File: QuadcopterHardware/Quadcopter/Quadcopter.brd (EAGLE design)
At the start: 47 x 28 mm, 47 parts, among them J2 FTDI_DEVICERA_SMT, M1 WIRELESS-NRF24L01, U1 ATMEGA328P_TQFP, U3 GY-521MPU6050

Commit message: getting there
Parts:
- removed J2: FTDI_DEVICERA_SMT, quad:FTDI_DEVICE_RA_SMT
- added J1: FTDI_DEVICE, quad:FTDI_DEVICE_SIDE
- moved C14 7.04 mm to (7.06, 30.6)
- moved R6 3.88 mm to (8.28, 15.5), turned to 90 degrees
- moved C9 3.01 mm to (6.21, 23.2)
- moved C6 2.19 mm to (6.25, 13.5), turned to 270 degrees
- moved S1 0.57 mm to (3.96, 6.59)
- moved U3 0.26 mm to (23.3, 16.0)
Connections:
- net 3V3: now also J1.P$4; no longer J2.4
- net DTR: now also J1.P$1; no longer J2.1
- net GND: now also J1.P$5, J1.P$6; no longer J2.5, J2.6
- net UART_RX: now also J1.P$3; no longer J2.3
- net UART_TX: now also J1.P$2; no longer J2.2
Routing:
- net RST: track 9.72 -> 36.7 mm, vias 0 -> 2
- net VBATT: track 73.2 -> 47.4 mm
- net ACC_INT: track 0.00 -> 21.7 mm
- net UART_RX: track 0.00 -> 18.4 mm, vias 0 -> 2
- net 3V3: track 77.6 -> 95.3 mm
- net UART_TX: track 0.00 -> 16.6 mm, vias 0 -> 2
- net DTR: track 11.6 -> 3.00 mm, vias 1 -> 0
- net SCL: track 0.00 -> 8.02 mm
- net SDA: track 0.00 -> 6.52 mm
- net GND: track 46.9 -> 44.3 mm

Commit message: draft 1 done, needs checking
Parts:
- removed LED2, LED3: RED, led:CHIP-LED0603
- removed R1, R3: 150, rcl:R0603
- moved LED1 58.8 mm to (27.1, 22.3)
- moved R4 56.8 mm to (32.2, 22.3)
- moved C14 7.42 mm to (6.21, 23.2), flipped to the bottom
- moved C6 3.21 mm to (8.98, 11.9)
- moved R6 2.90 mm to (6.12, 13.6)
- moved R8 1.56 mm to (35.8, 23.2)
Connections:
- removed net LED2: LED2.A, U1.25
- removed net LED3: LED3.A, U1.26
- removed net N$2: LED2.C, R3.1
- removed net N$3: LED3.C, R4.1
- removed net N$5: LED1.C, R1.1
- new net LEDRESISTOR: LED1.C, R4.1
- net GND: no longer R1.2, R3.2
- net LED1: now also U1.26; no longer U1.24
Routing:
- net 3V3: track 95.3 -> 112.7 mm, vias 2 -> 3
- net UART_TX: track 16.6 -> 25.7 mm
- net RST: track 36.7 -> 45.3 mm
- net UART_RX: track 18.4 -> 26.7 mm
- net GND: track 44.3 -> 48.5 mm
- net LEDRESISTOR: track 0.00 -> 3.52 mm
- net DTR: track 3.00 -> 5.03 mm
- net N$5: track 1.70 -> 0.00 mm
- net N$2: track 1.58 -> 0.00 mm
- net VDIV: track 7.76 -> 9.30 mm
- net ACC_INT: track 21.7 -> 20.2 mm
- net N$3: track 1.49 -> 0.00 mm
- net LED1: track 0.00 -> 1.37 mm

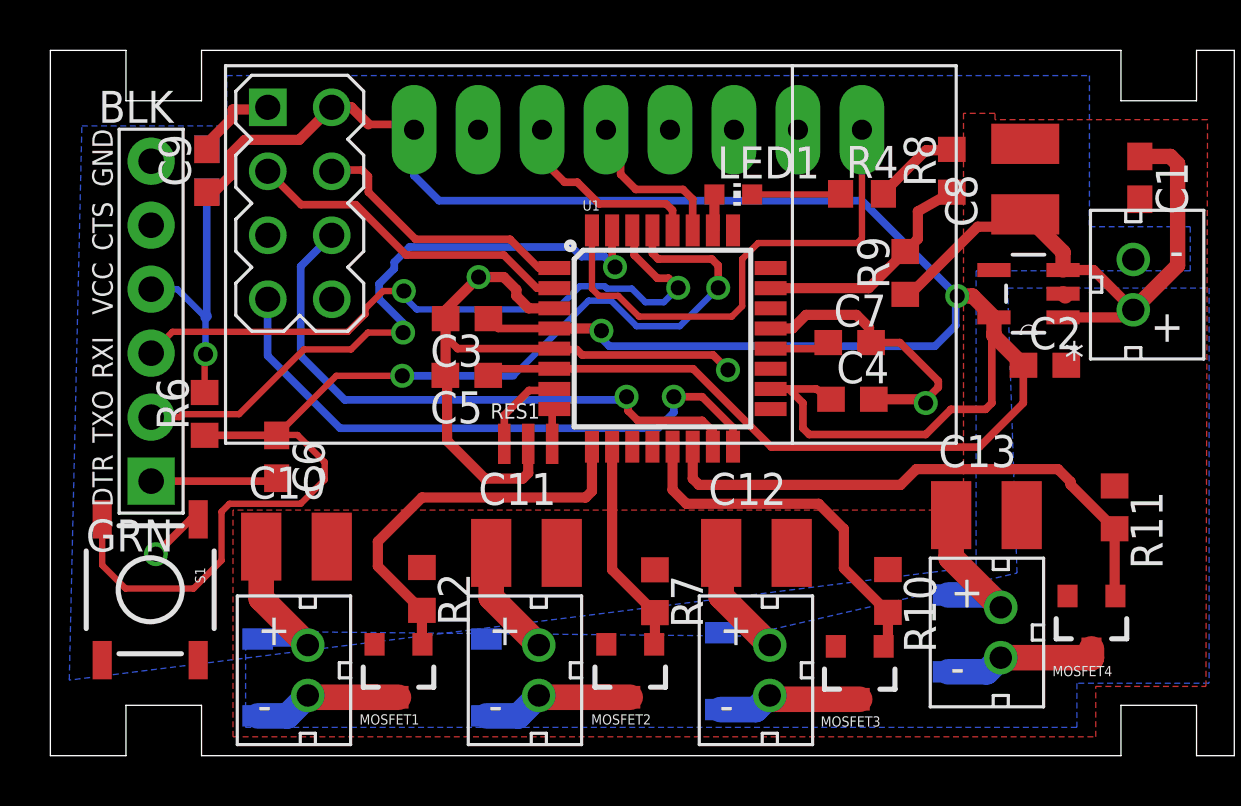
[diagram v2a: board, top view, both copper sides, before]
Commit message: routed unrouted airwires
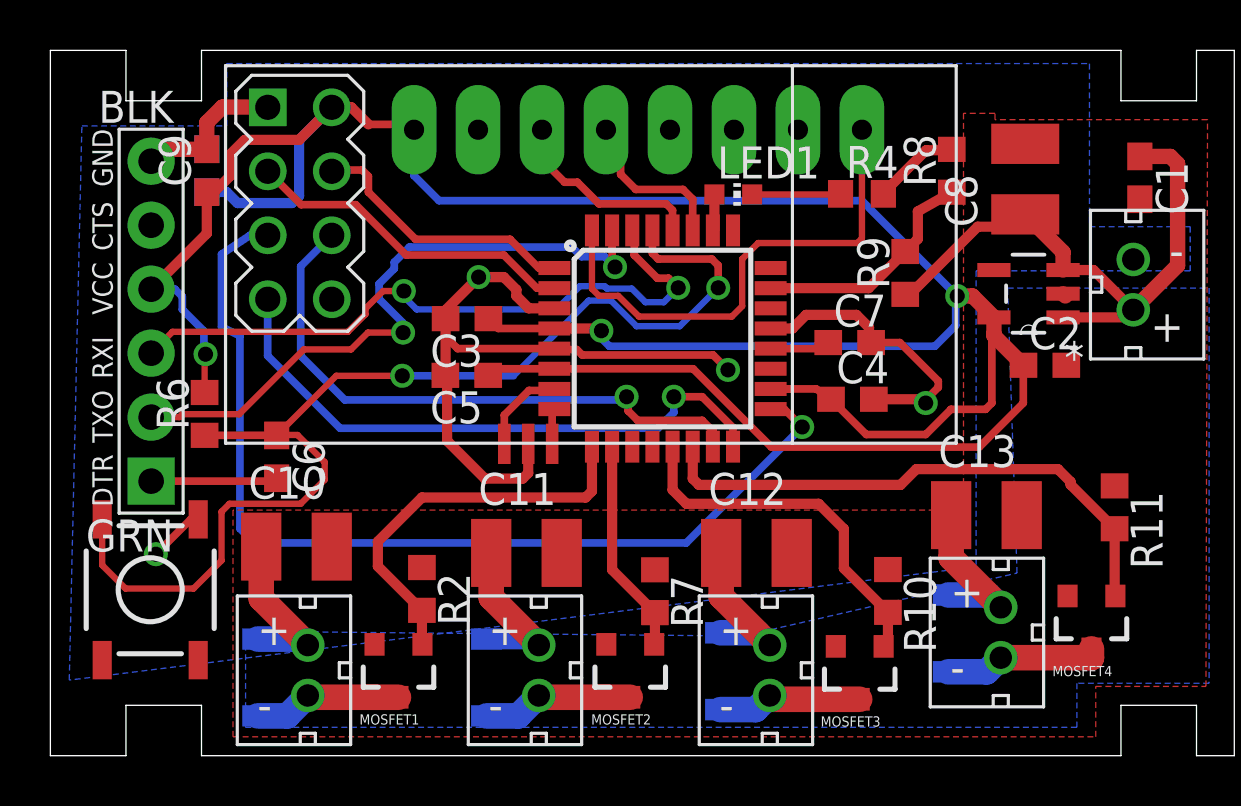
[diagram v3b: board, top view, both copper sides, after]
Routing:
- net SCK: track 0.00 -> 39.4 mm, vias 0 -> 1
- net 3V3: track 112.7 -> 118.0 mm
- net VBATT: track 47.4 -> 50.7 mm
- net GND: track 48.5 -> 51.2 mm
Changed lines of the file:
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@@
 <param name="RoutingGrid" value="50mil"/>
 <param name="AutoGrid" value="1"/>
-<param name="Efforts" value="0"/>
+<param name="Efforts" value="2"/>
 <param name="TopRouterVariant" value="1"/>
 <param name="tpViaShape" value="round"/>
@@
 <element name="R8" library="rcl" package="R0603" value="1K" x="35.78525" y="23.2195" rot="R90"/>
 <element name="R9" library="rcl" package="R0603" value="1.7K" x="33.9375" y="19.165" rot="R90"/>
-<element name="RES1" library="quad" package="CSTCE16M0V53-R0" value="CSTCE10M0G55-R0" x="18.97" y="12.38" rot="R270"/>
-<element name="S1" library="quad" package="TACTILE-SWITCH-SMD" value="SWITCH-MOMENTARY-2SMD" x="3.9625" y="6.5875" rot="R270">
+<element name="RES1" library="quad" package="CSTCE16M0V53-R0" value="CSTCE10M0G55-R0" x="18.97" y="12.38" smashed="yes" rot="R270"/>
+<element name="S1" library="quad" package="TACTILE-SWITCH-SMD" value="SWITCH-MOMENTARY-2SMD" x="3.9625" y="6.5875" smashed="yes" rot="R270">
 <attribute name="PROD_ID" value="SWCH-08247" x="3.9625" y="6.5875" size="1.778" layer="27" rot="R270" display="off"/>
 </element>
@@
 </element>
 <element name="U$2" library="quad" package="JST_CONNECTOR_FEMALE" value="JST_Battery" x="42.99" y="18.7" rot="R180"/>
-<element name="U1" library="quad" package="TQFP32-08" value="ATMEGA328P_TQFP" x="24.3" y="16.56">
+<element name="U1" library="quad" package="TQFP32-08" value="ATMEGA328P_TQFP" x="24.3" y="16.56" smashed="yes">
 <attribute name="PROD_ID" value="IC-09069" x="24.3" y="16.56" size="1.778" layer="27" display="off"/>
 </element>
 <element name="U3" library="quad" package="GY-521" value="GY-521MPU6050" x="23.3275" y="15.96" rot="MR270"/>
-<element name="J1" library="quad" package="FTDI_DEVICE_SIDE" value="FTDI_DEVICE" x="4" y="17.25" rot="R90"/>
+<element name="J1" library="quad" package="FTDI_DEVICE_SIDE" value="FTDI_DEVICE" x="4" y="17.25" smashed="yes" rot="R90"/>
 </elements>
 <signals>
@@
 <contactref element="U$2" pad="+"/>
 <wire x1="38.4702" y1="21.2602" x2="38.7" y2="21.49" width="0.8128" layer="1"/>
-<wire x1="9.98" y1="4.63" x2="10.22" y2="4.39" width="1.016" layer="16"/>
-<wire x1="19.15" y1="4.63" x2="19.39" y2="4.39" width="1.016" layer="16"/>
-<wire x1="28.07" y1="4.88" x2="28.56" y2="4.39" width="1.016" layer="16"/>
 <wire x1="35.64" y1="6.38" x2="37.24" y2="6.38" width="1.016" layer="16"/>
 <wire x1="37.24" y1="6.38" x2="37.73" y2="5.89" width="1.016" layer="16"/>
@@
 <vertex x="38.375" y="7.25"/>
 </polygon>
-<wire x1="8.23" y1="4.63" x2="9.98" y2="4.63" width="0.6096" layer="16"/>
-<wire x1="26.6" y1="4.88" x2="26.63" y2="6.32" width="0" layer="19" extent="1-16"/>
-<wire x1="17.31" y1="4.63" x2="17.5" y2="6.28" width="0" layer="19" extent="1-16"/>
+<wire x1="8.23" y1="4.63" x2="9.98" y2="4.63" width="1.016" layer="16"/>
+<wire x1="17.31" y1="4.63" x2="19.15" y2="4.63" width="0.8128" layer="16"/>
+<wire x1="9.98" y1="4.63" x2="10.22" y2="4.39" width="0.8128" layer="16"/>
+<wire x1="19.15" y1="4.63" x2="19.39" y2="4.39" width="1.016" layer="16"/>
+<wire x1="26.6" y1="4.88" x2="28.07" y2="4.88" width="1.016" layer="16"/>
+<wire x1="28.07" y1="4.88" x2="28.56" y2="4.39" width="0.8128" layer="16"/>
 </signal>
 <signal name="GND">
@@
 <contactref element="R8" pad="2"/>
 <wire x1="40.2916" y1="18.25" x2="40.2016" y2="18.34" width="0.6096" layer="1"/>
-<polygon width="0.4064" layer="1">
+<polygon width="0.4064" layer="1" isolate="0.3048">
 <vertex x="36.25" y="25.5"/>
 <vertex x="36.25" y="9.75"/>
@@
 <vertex x="37.5" y="25.5"/>
 </polygon>
-<polygon width="0.4064" layer="16" rank="2">
+<polygon width="0.4064" layer="16" isolate="0.3048" rank="2">
 <vertex x="1.25" y="25"/>
 <vertex x="7" y="25"/>
-<vertex x="7" y="27"/>
-<vertex x="41.25" y="27"/>
+<vertex x="7" y="27.47625"/>
+<vertex x="41.25" y="27.47625"/>
 <vertex x="41.25" y="21"/>
 <vertex x="45.25" y="21"/>
@@
 <wire x1="20.8955" y1="16.125" x2="21.11375" y2="15.90675" width="0.3048" layer="1"/>
 <wire x1="21.11375" y1="15.90675" x2="26.30775" y2="15.90675" width="0.3048" layer="1"/>
-<wire x1="6.2105" y1="24.07225" x2="6.2105" y2="24.308" width="0.4064" layer="1"/>
-<wire x1="6.2105" y1="24.308" x2="7.239" y2="25.3365" width="0.4064" layer="1"/>
-<wire x1="7.239" y1="25.3365" x2="7.239" y2="25.654" width="0.4064" layer="1"/>
-<wire x1="7.239" y1="25.654" x2="8.544" y2="25.654" width="0.4064" layer="1"/>
-<wire x1="8.544" y1="25.654" x2="8.63" y2="25.74" width="0.4064" layer="1"/>
 <wire x1="33.06975" y1="22.30275" x2="33.06975" y2="22.33825" width="0.4064" layer="1"/>
 <wire x1="33.06975" y1="22.33825" x2="34.76625" y2="24.03475" width="0.4064" layer="1"/>
 <wire x1="34.76625" y1="24.03475" x2="35.7505" y2="24.03475" width="0.4064" layer="1"/>
 <wire x1="35.7505" y1="24.03475" x2="35.78525" y2="24.0695" width="0.4064" layer="1"/>
-<wire x1="18.75" y1="11" x2="20.3" y2="8.05" width="0" layer="19" extent="1-1"/>
+<wire x1="6.2105" y1="24.07225" x2="4.47225" y2="24.07225" width="0.6096" layer="1"/>
+<wire x1="4.47225" y1="24.07225" x2="4" y2="23.6" width="0.6096" layer="1"/>
+<wire x1="6.2105" y1="24.07225" x2="6.2105" y2="25.1335" width="0.6096" layer="1"/>
+<wire x1="6.2105" y1="25.1335" x2="6.82625" y2="25.74925" width="0.6096" layer="1"/>
+<wire x1="6.82625" y1="25.74925" x2="8.62075" y2="25.74925" width="0.6096" layer="1"/>
+<wire x1="8.62075" y1="25.74925" x2="8.63" y2="25.74" width="0.6096" layer="1"/>
 </signal>
 <signal name="3V3">
@@
 <wire x1="20.0074" y1="16.96" x2="19.46" y2="16.96" width="0.3048" layer="1"/>
 <wire x1="28.5926" y1="14.56" x2="29.315" y2="14.56" width="0.3048" layer="1"/>
-<wire x1="29.315" y1="14.56" x2="29.875" y2="14" width="0.3048" layer="1"/>
-<wire x1="29.875" y1="14" x2="29.875" y2="13" width="0.3048" layer="1"/>
-<wire x1="29.875" y1="13" x2="30.125" y2="12.75" width="0.3048" layer="1"/>
-<wire x1="30.125" y1="12.75" x2="34.75" y2="12.75" width="0.3048" layer="1"/>
 <wire x1="34.75" y1="12.75" x2="35.75" y2="13.75" width="0.3048" layer="1"/>
 <wire x1="35.75" y1="13.75" x2="37.125" y2="13.75" width="0.3048" layer="1"/>
@@
 <wire x1="6.12325" y1="14.4185" x2="6.12325" y2="15.90225" width="0.254" layer="1"/>
 <wire x1="6.12325" y1="15.90225" x2="6.1595" y2="15.9385" width="0.254" layer="1"/>
-<wire x1="4" y1="18.52" x2="5.0385" y2="18.52" width="0.254" layer="16"/>
-<wire x1="5.0385" y1="18.52" x2="6.1595" y2="17.399" width="0.254" layer="16"/>
-<wire x1="6.1595" y1="17.399" x2="6.1595" y2="15.9385" width="0.254" layer="16"/>
 <wire x1="6.2105" y1="22.37225" x2="6.49725" y2="22.37225" width="0.4064" layer="1"/>
 <wire x1="6.49725" y1="22.37225" x2="7.14375" y2="23.01875" width="0.4064" layer="1"/>
@@
 <wire x1="7.71525" y1="24.4475" x2="9.8775" y2="24.4475" width="0.4064" layer="1"/>
 <wire x1="9.8775" y1="24.4475" x2="11.17" y2="25.74" width="0.4064" layer="1"/>
-<wire x1="6.209" y1="22.379" x2="6.209" y2="17.4485" width="0.3048" layer="16"/>
-<wire x1="6.209" y1="17.4485" x2="6.1595" y2="17.399" width="0.4064" layer="16"/>
-<wire x1="6.209" y1="22.379" x2="6.2105" y2="22.37225" width="0" layer="19" extent="1-16"/>
+<wire x1="34.75" y1="12.75" x2="32.39" y2="12.75" width="0.3048" layer="1"/>
+<wire x1="32.39" y1="12.75" x2="30.99" y2="14.15" width="0.3048" layer="1"/>
+<wire x1="4" y1="18.52" x2="4.94325" y2="18.52" width="0.3048" layer="16"/>
+<wire x1="4.94325" y1="18.52" x2="5.23875" y2="18.2245" width="0.3048" layer="16"/>
+<wire x1="5.23875" y1="18.2245" x2="5.23875" y2="17.7165" width="0.3048" layer="16"/>
+<wire x1="5.23875" y1="17.7165" x2="6.096" y2="16.85925" width="0.3048" layer="16"/>
+<wire x1="6.096" y1="16.85925" x2="6.096" y2="16.002" width="0.3048" layer="16"/>
+<wire x1="6.096" y1="16.002" x2="6.1595" y2="15.9385" width="0.3048" layer="16"/>
+<wire x1="6.209" y1="22.379" x2="6.98975" y2="22.379" width="0.4064" layer="16"/>
+<wire x1="6.98975" y1="22.379" x2="7.4295" y2="21.93925" width="0.4064" layer="16"/>
+<wire x1="7.4295" y1="21.93925" x2="9.5885" y2="21.93925" width="0.4064" layer="16"/>
+<wire x1="9.5885" y1="21.93925" x2="9.87425" y2="22.225" width="0.4064" layer="16"/>
+<wire x1="9.87425" y1="22.225" x2="9.87425" y2="24.44425" width="0.4064" layer="16"/>
+<wire x1="9.87425" y1="24.44425" x2="11.17" y2="25.74" width="0.4064" layer="16"/>
+<wire x1="6.2105" y1="22.37225" x2="6.2105" y2="20.7305" width="0.4064" layer="1"/>
+<wire x1="6.2105" y1="20.7305" x2="4" y2="18.52" width="0.4064" layer="1"/>
 </signal>
 <signal name="RST">
@@
 <contactref element="U1" pad="17"/>
 <contactref element="M1" pad="5"/>
-<wire x1="8.63" y1="20.66" x2="28.5926" y2="13.76" width="0" layer="19" extent="1-1"/>
+<via x="29.845" y="13.04925" extent="1-16" drill="0.6"/>
+<wire x1="28.5926" y1="13.76" x2="29.13425" y2="13.76" width="0.3048" layer="1"/>
+<wire x1="29.13425" y1="13.76" x2="29.845" y2="13.04925" width="0.3048" layer="1"/>
+<wire x1="8.63" y1="20.66" x2="7.92825" y2="20.66" width="0.3048" layer="16"/>
+<wire x1="7.92825" y1="20.66" x2="6.7945" y2="19.90725" width="0.3048" layer="16"/>
+<wire x1="6.7945" y1="19.90725" x2="6.7945" y2="17.018" width="0.3048" layer="16"/>
+<wire x1="6.7945" y1="17.018" x2="7.52475" y2="16.66875" width="0.3048" layer="16"/>
+<wire x1="7.52475" y1="16.66875" x2="7.52475" y2="9.017" width="0.3048" layer="16"/>
+<wire x1="7.52475" y1="9.017" x2="8.09625" y2="8.4455" width="0.3048" layer="16"/>
+<wire x1="8.09625" y1="8.4455" x2="25.24125" y2="8.4455" width="0.3048" layer="16"/>
+<wire x1="25.24125" y1="8.4455" x2="29.845" y2="13.04925" width="0.3048" layer="16"/>
 </signal>
 <signal name="MOSI">
@@
 <contactref element="LED1" pad="A"/>
 <wire x1="26.36075" y1="22.28025" x2="26.36075" y2="20.91335" width="0.4064" layer="1"/>
-<wire x1="26.36075" y1="20.91335" x2="26.3" y2="20.8526" width="0" layer="19" extent="1-1"/>
+<wire x1="26.36075" y1="20.91335" x2="26.3" y2="20.8526" width="0.3048" layer="1"/>
 </signal>
 </signals>
